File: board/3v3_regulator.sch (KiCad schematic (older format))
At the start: 8 parts

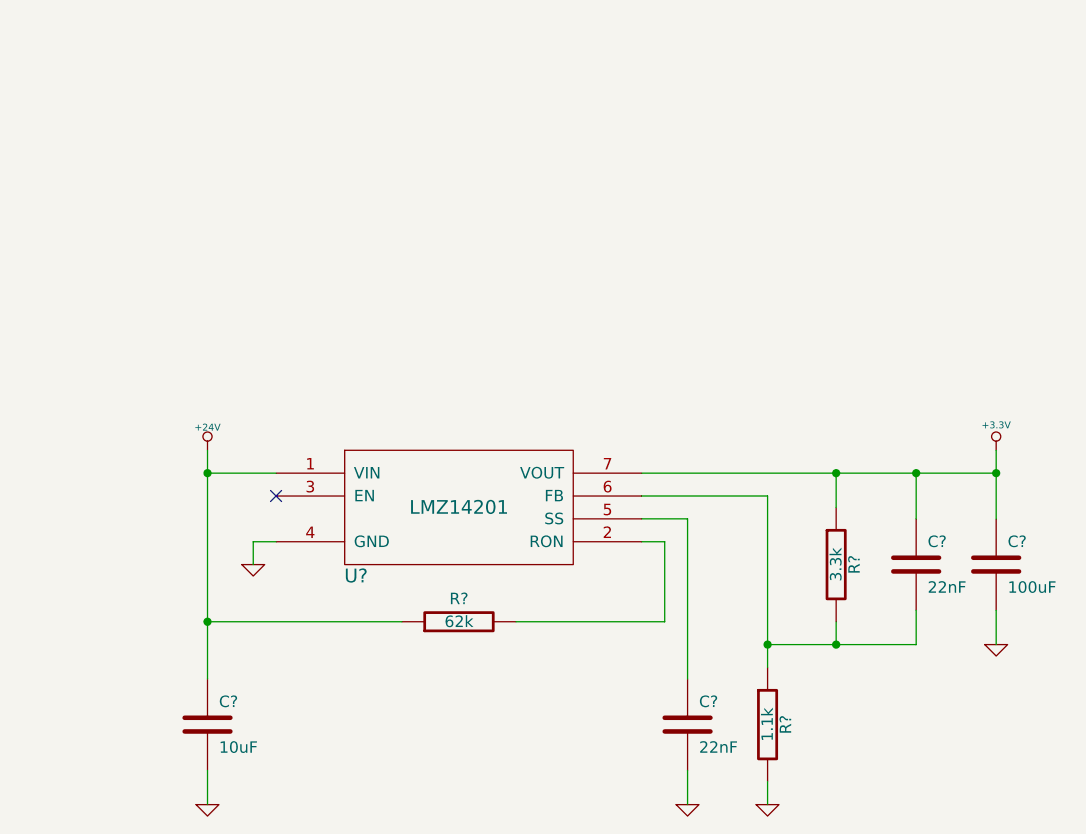
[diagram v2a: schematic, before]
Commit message: Decoupled analog section with an inductor.
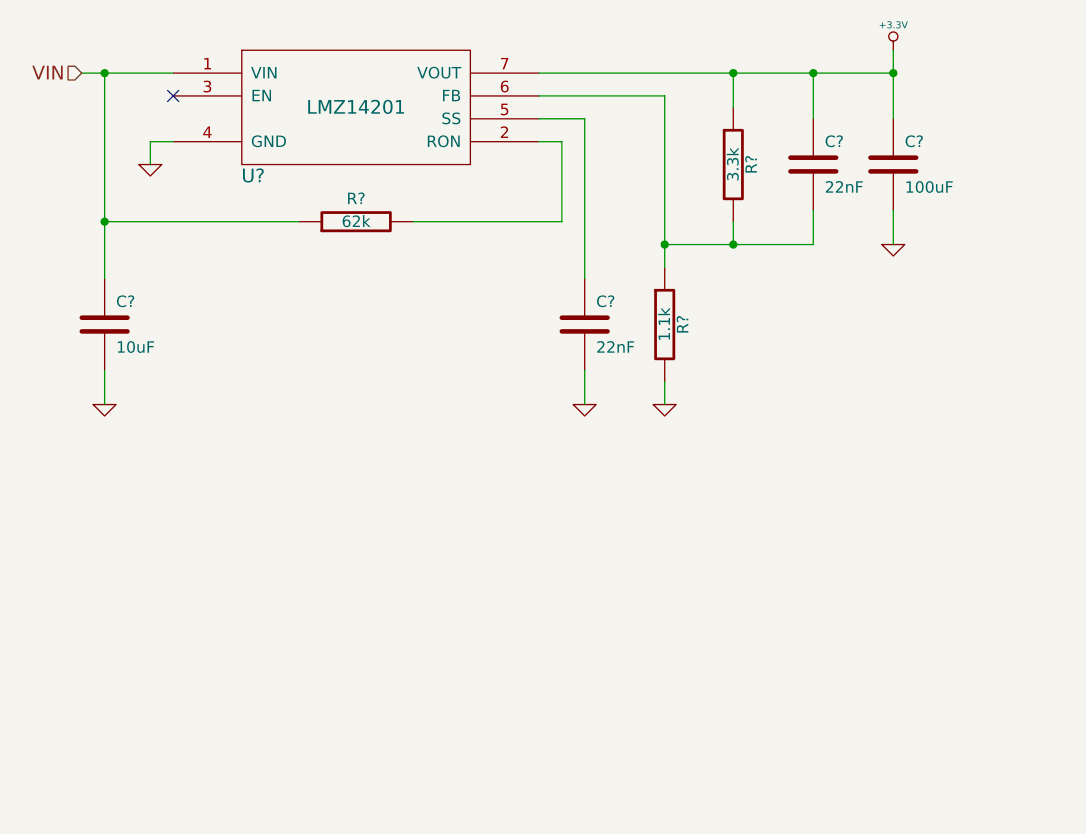
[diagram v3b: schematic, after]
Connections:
- net +24V renamed VIN
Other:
- moved on the sheet: C?, R?, U?

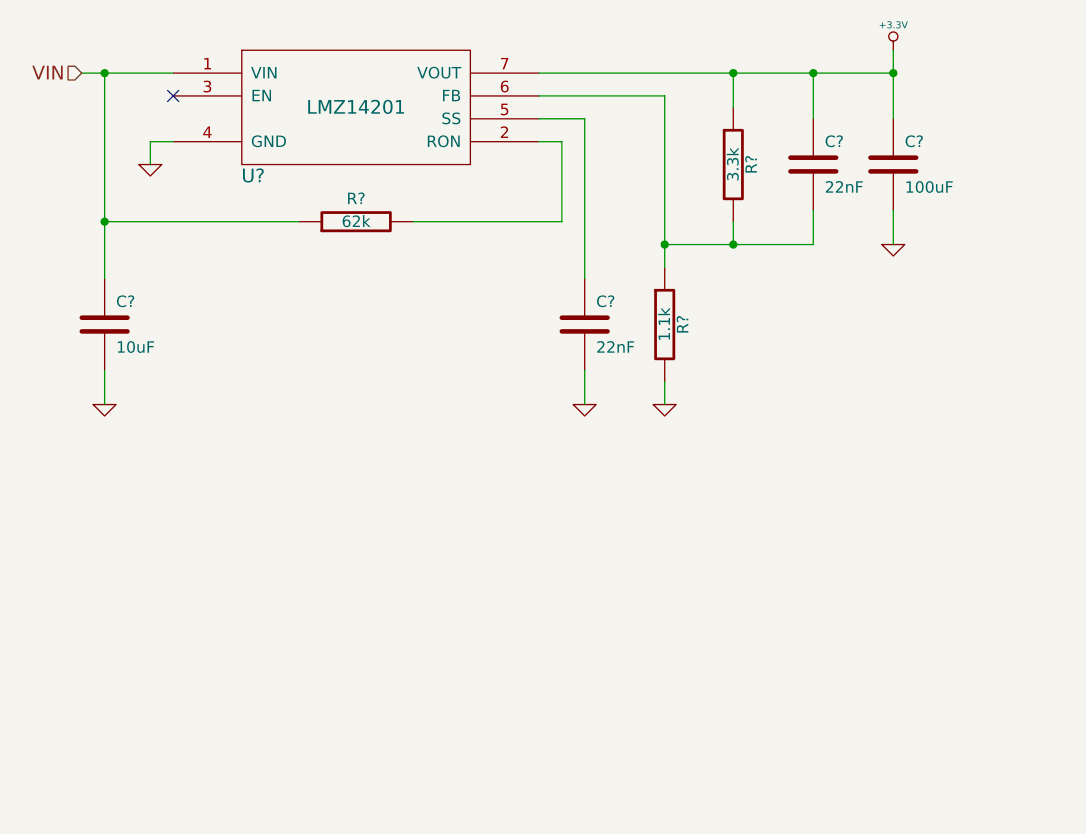
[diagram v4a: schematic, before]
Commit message: Fixed ERC Errors. Annotated all components.
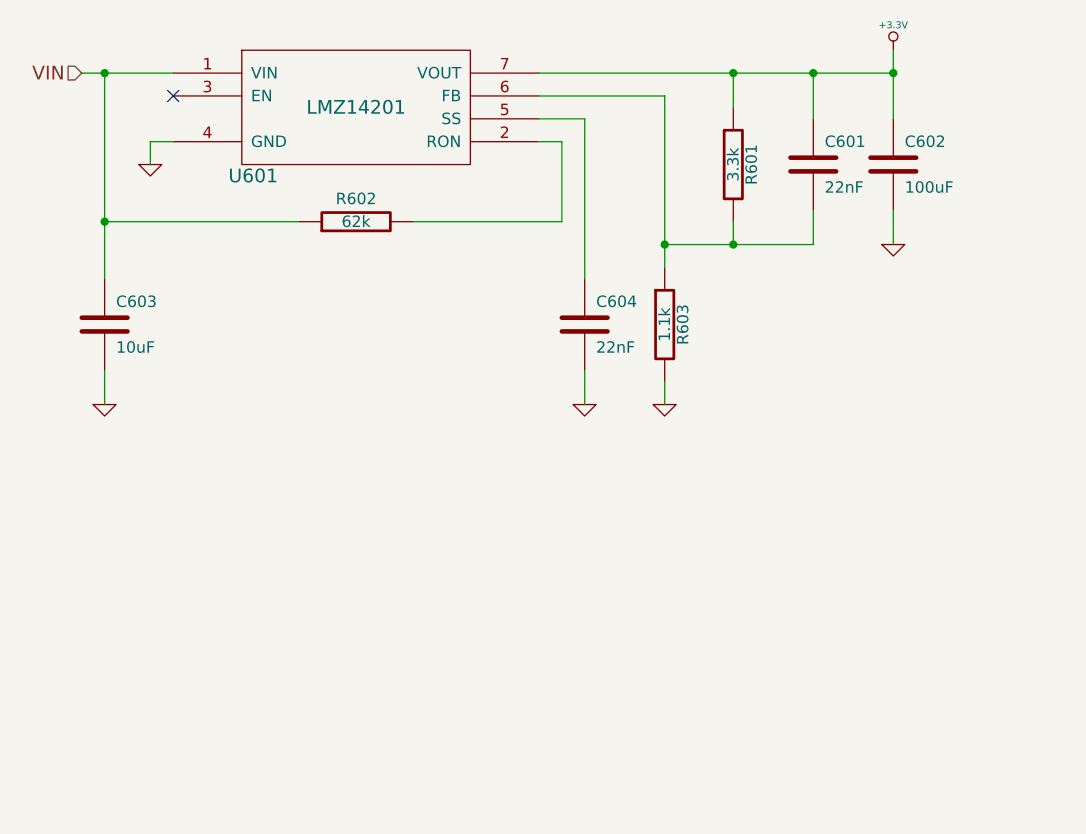
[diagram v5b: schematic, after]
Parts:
- gave numbers to parts that had none: 8
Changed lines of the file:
@@
 $EndDescr
 $Comp
-L GND #PWR?
+L GND #PWR0130
 U 1 1 52E6BE42
 P 4150 3500
-F 0 "#PWR?" H 4150 3500 30  0001 C CNN
+F 0 "#PWR0130" H 4150 3500 30  0001 C CNN
 F 1 "GND" H 4150 3430 30  0001 C CNN
 F 2 "" H 4150 3500 60  0000 C CNN
@@
 NoConn ~ 4250 3200
 $Comp
-L +3.3V #PWR?
+L +3.3V #PWR0131
 U 1 1 52E6BFC0
 P 7400 3000
-F 0 "#PWR?" H 7400 2960 30  0001 C CNN
+F 0 "#PWR0131" H 7400 2960 30  0001 C CNN
 F 1 "+3.3V" H 7400 3110 30  0000 C CNN
 F 2 "" H 7400 3000 60  0000 C CNN
@@
 	7400 3000 7400 3300
 $Comp
-L R R?
+L R R602
 U 1 1 52E6C146
 P 5050 3750
-F 0 "R?" V 5150 3750 50  0000 C CNN
+F 0 "R602" V 5150 3750 50  0000 C CNN
 F 1 "62k" V 5050 3750 50  0000 C CNN
 F 2 "" H 5050 3750 60  0000 C CNN
@@
 $EndComp
 $Comp
-L C C?
+L C C603
 U 1 1 52E6C23B
 P 3950 4200
-F 0 "C?" H 4000 4300 50  0000 L CNN
+F 0 "C603" H 4000 4300 50  0000 L CNN
 F 1 "10uF" H 4000 4100 50  0000 L CNN
 F 2 "" H 3950 4200 60  0000 C CNN
@@
 $EndComp
 $Comp
-L GND #PWR?
+L GND #PWR0132
 U 1 1 52E6C24F
 P 3950 4550
-F 0 "#PWR?" H 3950 4550 30  0001 C CNN
+F 0 "#PWR0132" H 3950 4550 30  0001 C CNN
 F 1 "GND" H 3950 4480 30  0001 C CNN
 F 2 "" H 3950 4550 60  0000 C CNN
@@
 	3950 4400 3950 4550
 $Comp
-L C C?
+L C C604
 U 1 1 52E6C2A8
 P 6050 4200
-F 0 "C?" H 6100 4300 50  0000 L CNN
+F 0 "C604" H 6100 4300 50  0000 L CNN
 F 1 "22nF" H 6100 4100 50  0000 L CNN
 F 2 "" H 6050 4200 60  0000 C CNN
@@
 $EndComp
 $Comp
-L GND #PWR?
+L GND #PWR0133
 U 1 1 52E6C2C8
 P 6050 4550
-F 0 "#PWR?" H 6050 4550 30  0001 C CNN
+F 0 "#PWR0133" H 6050 4550 30  0001 C CNN
 F 1 "GND" H 6050 4480 30  0001 C CNN
 F 2 "" H 6050 4550 60  0000 C CNN
@@
 	6050 4400 6050 4550
 $Comp
-L R R?
+L R R603
 U 1 1 52E6C482
 P 6400 4200
-F 0 "R?" V 6480 4200 50  0000 C CNN
+F 0 "R603" V 6480 4200 50  0000 C CNN
 F 1 "1.1k" V 6400 4200 50  0000 C CNN
 F 2 "" H 6400 4200 60  0000 C CNN
@@
 $EndComp
 $Comp
-L GND #PWR?
+L GND #PWR0134
 U 1 1 52E6C5D9
 P 6400 4550
-F 0 "#PWR?" H 6400 4550 30  0001 C CNN
+F 0 "#PWR0134" H 6400 4550 30  0001 C CNN
 F 1 "GND" H 6400 4480 30  0001 C CNN
 F 2 "" H 6400 4550 60  0000 C CNN
@@
 Connection ~ 3950 3100
 $Comp
-L LMZ14201 U?
+L LMZ14201 U601
 U 1 1 52E6C713
 P 5050 3250
-F 0 "U?" H 4600 2950 60  0000 C CNN
+F 0 "U601" H 4600 2950 60  0000 C CNN
 F 1 "LMZ14201" H 5050 3250 60  0000 C CNN
 F 2 "" H 5050 3250 60  0000 C CNN
@@
 	6400 3200 6400 3950
 $Comp
-L C C?
+L C C602
 U 1 1 52E6C927
 P 7400 3500
-F 0 "C?" H 7450 3600 50  0000 L CNN
+F 0 "C602" H 7450 3600 50  0000 L CNN
 F 1 "100uF" H 7450 3400 50  0000 L CNN
 F 2 "" H 7400 3500 60  0000 C CNN
@@
 $EndComp
 $Comp
-L GND #PWR?
+L GND #PWR0135
 U 1 1 52E6C951
 P 7400 3850
-F 0 "#PWR?" H 7400 3850 30  0001 C CNN
+F 0 "#PWR0135" H 7400 3850 30  0001 C CNN
 F 1 "GND" H 7400 3780 30  0001 C CNN
 F 2 "" H 7400 3850 60  0000 C CNN
@@
 	6400 4450 6400 4550
 $Comp
-L C C?
+L C C601
 U 1 1 52E6C9C8
 P 7050 3500
-F 0 "C?" H 7100 3600 50  0000 L CNN
+F 0 "C601" H 7100 3600 50  0000 L CNN
 F 1 "22nF" H 7100 3400 50  0000 L CNN
 F 2 "" H 7050 3500 60  0000 C CNN
@@
 $EndComp
 $Comp
-L R R?
+L R R601
 U 1 1 52E6C9DC
 P 6700 3500
-F 0 "R?" V 6780 3500 50  0000 C CNN
+F 0 "R601" V 6780 3500 50  0000 C CNN
 F 1 "3.3k" V 6700 3500 50  0000 C CNN
 F 2 "" H 6700 3500 60  0000 C CNN

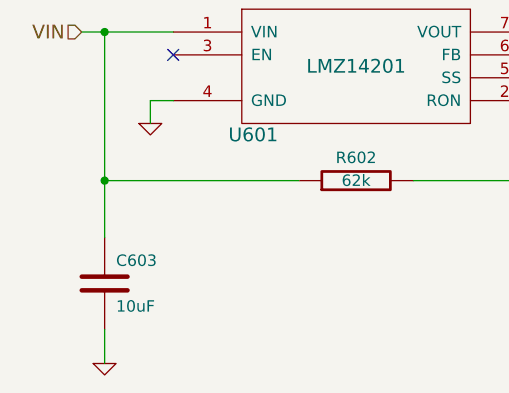
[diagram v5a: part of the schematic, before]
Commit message: Selected Part Numbers for all Components
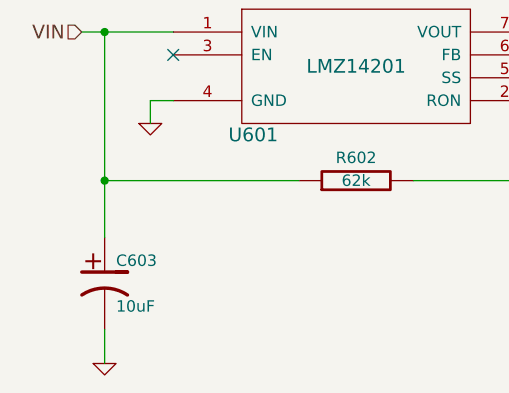
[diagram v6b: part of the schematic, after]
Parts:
- removed C603: 10uF, symbol C
- added C603: 10uF, symbol CP1
- C601, C604: Part Number (none) -> CL10B222KB8NCNC
- C602: Part Number (none) -> C1206C107M9PACTU
- R601: Part Number (none) -> MCR03ERTF3301
- R602: Part Number (none) -> RC1608J623CS
- R603: Part Number (none) -> MCR03ERTF1101
- U601: Part Number (none) -> LMZ14201
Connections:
- net GND: now also C603.2
- net VIN: now also C603.1
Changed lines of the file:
@@
 $Descr A 11000 8500
 encoding utf-8
-Sheet 10 26
+Sheet 6 26
 Title "3.3V Switching Regulator"
 Date "21 jan 2014"
@@
 $EndDescr
 $Comp
-L GND #PWR0130
+L GND #PWR0135
 U 1 1 52E6BE42
 P 4150 3500
-F 0 "#PWR0130" H 4150 3500 30  0001 C CNN
+F 0 "#PWR0135" H 4150 3500 30  0001 C CNN
 F 1 "GND" H 4150 3430 30  0001 C CNN
 F 2 "" H 4150 3500 60  0000 C CNN
@@
 NoConn ~ 4250 3200
 $Comp
-L +3.3V #PWR0131
+L +3.3V #PWR0136
 U 1 1 52E6BFC0
 P 7400 3000
-F 0 "#PWR0131" H 7400 2960 30  0001 C CNN
+F 0 "#PWR0136" H 7400 2960 30  0001 C CNN
 F 1 "+3.3V" H 7400 3110 30  0000 C CNN
 F 2 "" H 7400 3000 60  0000 C CNN
@@
 F 2 "" H 5050 3750 60  0000 C CNN
 F 3 "" H 5050 3750 60  0000 C CNN
+F 4 "RC1608J623CS" V 5050 3750 60  0001 C CNN "Part Number"
 	1    5050 3750
 	0    -1   -1   0
 $EndComp
 $Comp
-L C C603
-U 1 1 52E6C23B
-P 3950 4200
-F 0 "C603" H 4000 4300 50  0000 L CNN
-F 1 "10uF" H 4000 4100 50  0000 L CNN
-F 2 "" H 3950 4200 60  0000 C CNN
-F 3 "" H 3950 4200 60  0000 C CNN
-	1    3950 4200
-	1    0    0    -1
-$EndComp
-$Comp
-L GND #PWR0132
+L GND #PWR0137
 U 1 1 52E6C24F
 P 3950 4550
-F 0 "#PWR0132" H 3950 4550 30  0001 C CNN
+F 0 "#PWR0137" H 3950 4550 30  0001 C CNN
 F 1 "GND" H 3950 4480 30  0001 C CNN
 F 2 "" H 3950 4550 60  0000 C CNN
@@
 F 2 "" H 6050 4200 60  0000 C CNN
 F 3 "" H 6050 4200 60  0000 C CNN
+F 4 "CL10B222KB8NCNC" H 6050 4200 60  0001 C CNN "Part Number"
 	1    6050 4200
 	1    0    0    -1
 $EndComp
 $Comp
-L GND #PWR0133
+L GND #PWR0138
 U 1 1 52E6C2C8
 P 6050 4550
-F 0 "#PWR0133" H 6050 4550 30  0001 C CNN
+F 0 "#PWR0138" H 6050 4550 30  0001 C CNN
 F 1 "GND" H 6050 4480 30  0001 C CNN
 F 2 "" H 6050 4550 60  0000 C CNN
@@
 F 2 "" H 6400 4200 60  0000 C CNN
 F 3 "" H 6400 4200 60  0000 C CNN
+F 4 "MCR03ERTF1101" V 6400 4200 60  0001 C CNN "Part Number"
 	1    6400 4200
 	1    0    0    -1
 $EndComp
 $Comp
-L GND #PWR0134
+L GND #PWR0139
 U 1 1 52E6C5D9
 P 6400 4550
-F 0 "#PWR0134" H 6400 4550 30  0001 C CNN
+F 0 "#PWR0139" H 6400 4550 30  0001 C CNN
 F 1 "GND" H 6400 4480 30  0001 C CNN
 F 2 "" H 6400 4550 60  0000 C CNN
@@
 F 2 "" H 5050 3250 60  0000 C CNN
 F 3 "" H 5050 3250 60  0000 C CNN
+F 4 "LMZ14201" H 5050 3250 60  0001 C CNN "Part Number"
 	1    5050 3250
 	1    0    0    -1
@@
 F 2 "" H 7400 3500 60  0000 C CNN
 F 3 "" H 7400 3500 60  0000 C CNN
+F 4 "C1206C107M9PACTU" H 7400 3500 60  0001 C CNN "Part Number"
 	1    7400 3500
 	1    0    0    -1
 $EndComp
 $Comp
-L GND #PWR0135
+L GND #PWR0140
 U 1 1 52E6C951
 P 7400 3850
-F 0 "#PWR0135" H 7400 3850 30  0001 C CNN
+F 0 "#PWR0140" H 7400 3850 30  0001 C CNN
 F 1 "GND" H 7400 3780 30  0001 C CNN
 F 2 "" H 7400 3850 60  0000 C CNN
@@
 F 2 "" H 7050 3500 60  0000 C CNN
 F 3 "" H 7050 3500 60  0000 C CNN
+F 4 "CL10B222KB8NCNC" H 7050 3500 60  0001 C CNN "Part Number"
 	1    7050 3500
 	1    0    0    -1
@@
 F 2 "" H 6700 3500 60  0000 C CNN
 F 3 "" H 6700 3500 60  0000 C CNN
+F 4 "MCR03ERTF3301" V 6700 3500 60  0001 C CNN "Part Number"
 	1    6700 3500
 	1    0    0    -1
@@
 Wire Wire Line
 	3950 3100 3950 4000
+$Comp
+L CP1 C603
+U 1 1 5301A0DF
+P 3950 4200
+F 0 "C603" H 4000 4300 50  0000 L CNN
+F 1 "10uF" H 4000 4100 50  0000 L CNN
+F 2 "" H 3950 4200 60  0000 C CNN
+F 3 "" H 3950 4200 60  0000 C CNN
+F 4 "EEE-2AA100UP" H 3950 4200 60  0001 C CNN "Part Number"
+	1    3950 4200
+	1    0    0    -1
+$EndComp
 $EndSCHEMATC

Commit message: Digikey Number + Link
Added a digikey part number and link to all components.
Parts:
- C601, C604: Digikey Number (none) -> 1276-1989-1-ND; Part Number CL10B222KB8NCNC -> (none)
- C602: Digikey Number (none) -> 399-5620-1-ND; Part Number C1206C107M9PACTU -> (none)
- C603: Digikey Number (none) -> PCE3966CT-ND; Part Number EEE-2AA100UP -> (none)
- R601: Digikey Number (none) -> RHM3.30KCFCT-ND; Part Number MCR03ERTF3301 -> (none)
- R602: Digikey Number (none) -> 1276-5105-1-ND; Part Number RC1608J623CS -> (none)
- R603: Digikey Number (none) -> RHM1.1KCFCT-ND; Part Number MCR03ERTF1101 -> (none)
- U601: Digikey Number (none) -> LMZ14201TZ-ADJ/NOPBCT-ND; Part Number LMZ14201 -> (none)
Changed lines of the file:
@@
 F 1 "62k" V 5050 3750 50  0000 C CNN
 F 2 "" H 5050 3750 60  0000 C CNN
-F 3 "" H 5050 3750 60  0000 C CNN
-F 4 "RC1608J623CS" V 5050 3750 60  0001 C CNN "Part Number"
+F 3 "http://www.digikey.ca/product-detail/en/RC1608J623CS/1276-5105-1-ND/3968077" H 5050 3750 60  0001 C CNN
+F 4 "1276-5105-1-ND" H 6900 4550 60  0001 C CNN "Digikey Number"
 	1    5050 3750
 	0    -1   -1   0
@@
 F 1 "22nF" H 6100 4100 50  0000 L CNN
 F 2 "" H 6050 4200 60  0000 C CNN
-F 3 "" H 6050 4200 60  0000 C CNN
-F 4 "CL10B222KB8NCNC" H 6050 4200 60  0001 C CNN "Part Number"
+F 3 "http://www.digikey.ca/product-detail/en/CL10B222KB8NCNC/1276-1989-1-ND/3890075" H 6050 4200 60  0001 C CNN
+F 4 "1276-1989-1-ND" H 6900 4550 60  0001 C CNN "Digikey Number"
 	1    6050 4200
 	1    0    0    -1
@@
 F 1 "1.1k" V 6400 4200 50  0000 C CNN
 F 2 "" H 6400 4200 60  0000 C CNN
-F 3 "" H 6400 4200 60  0000 C CNN
-F 4 "MCR03ERTF1101" V 6400 4200 60  0001 C CNN "Part Number"
+F 3 "http://www.digikey.ca/product-detail/en/MCR03ERTF1101/RHM1.1KCFCT-ND/4083910" H 6400 4200 60  0001 C CNN
+F 4 "RHM1.1KCFCT-ND" H 6900 4550 60  0001 C CNN "Digikey Number"
 	1    6400 4200
 	1    0    0    -1
@@
 F 1 "LMZ14201" H 5050 3250 60  0000 C CNN
 F 2 "" H 5050 3250 60  0000 C CNN
-F 3 "" H 5050 3250 60  0000 C CNN
-F 4 "LMZ14201" H 5050 3250 60  0001 C CNN "Part Number"
+F 3 "http://www.digikey.ca/product-detail/en/LMZ14201TZ-ADJ%2FNOPB/LMZ14201TZ-ADJ%2FNOPBCT-ND/2203761" H 5050 3250 60  0001 C CNN
+F 4 "LMZ14201TZ-ADJ/NOPBCT-ND" H 6900 4550 60  0001 C CNN "Digikey Number"
 	1    5050 3250
 	1    0    0    -1
@@
 F 1 "100uF" H 7450 3400 50  0000 L CNN
 F 2 "" H 7400 3500 60  0000 C CNN
-F 3 "" H 7400 3500 60  0000 C CNN
-F 4 "C1206C107M9PACTU" H 7400 3500 60  0001 C CNN "Part Number"
+F 3 "http://www.digikey.ca/product-detail/en/C1206C107M9PACTU/399-5620-1-ND/2057834" H 7400 3500 60  0001 C CNN
+F 4 "399-5620-1-ND" H 6900 4550 60  0001 C CNN "Digikey Number"
 	1    7400 3500
 	1    0    0    -1
@@
 F 1 "22nF" H 7100 3400 50  0000 L CNN
 F 2 "" H 7050 3500 60  0000 C CNN
-F 3 "" H 7050 3500 60  0000 C CNN
-F 4 "CL10B222KB8NCNC" H 7050 3500 60  0001 C CNN "Part Number"
+F 3 "http://www.digikey.ca/product-detail/en/CL10B222KB8NCNC/1276-1989-1-ND/3890075" H 7050 3500 60  0001 C CNN
+F 4 "1276-1989-1-ND" H 6900 4550 60  0001 C CNN "Digikey Number"
 	1    7050 3500
 	1    0    0    -1
@@
 F 1 "3.3k" V 6700 3500 50  0000 C CNN
 F 2 "" H 6700 3500 60  0000 C CNN
-F 3 "" H 6700 3500 60  0000 C CNN
-F 4 "MCR03ERTF3301" V 6700 3500 60  0001 C CNN "Part Number"
+F 3 "http://www.digikey.ca/product-detail/en/MCR03ERTF3301/RHM3.30KCFCT-ND/2796479" H 6700 3500 60  0001 C CNN
+F 4 "RHM3.30KCFCT-ND" H 6900 4550 60  0001 C CNN "Digikey Number"
 	1    6700 3500
 	1    0    0    -1
@@
 F 1 "10uF" H 4000 4100 50  0000 L CNN
 F 2 "" H 3950 4200 60  0000 C CNN
-F 3 "" H 3950 4200 60  0000 C CNN
-F 4 "EEE-2AA100UP" H 3950 4200 60  0001 C CNN "Part Number"
+F 3 "http://www.digikey.ca/product-detail/en/EEE-2AA100UP/PCE3966CT-ND/766342" H 3950 4200 60  0001 C CNN
+F 4 "PCE3966CT-ND" H 6900 4550 60  0001 C CNN "Digikey Number"
 	1    3950 4200
 	1    0    0    -1
